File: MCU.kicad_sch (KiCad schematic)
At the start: 7 parts, among them U2 Teensy4.0, U9 W25Q128JVSIQ TR

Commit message: Finalized schematic
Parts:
- added R18, R19: 5k, Resistor_SMD:R_0402_1005Metric, symbol Device:R
- added TP1 (x13): TestPoint, TestPoint:TestPoint_Pad_1.5x1.5mm, symbol Connector:TestPoint
- C24, C25: footprint (none) -> Capacitor_SMD:C_0402_1005Metric
- R14, R24, R25: footprint (none) -> Resistor_SMD:R_0402_1005Metric
- U2: footprint (none) -> teensy:Teensy41
- U9: footprint SOIC_208MIL_WIN -> TeenieWeenieLibrary:SOIC_208MIL_WIN
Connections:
- net GNDD is gone; now on net GND: U9.4 (GND)
- net +3V3: now also R18.1, R19.1
- net ADCDAT: now also TP1.1
- net BCLK: now also TP1.1
- net CODC_IRQ: now also TP1.1
- net DACDAT: now also TP1.1
- net GND: now also U2.1 (GND)
- net MCLK: now also TP1.1
- net SCL: now also TP1.1
- net SDA: now also TP1.1
- net ~{ADC_IRQ0}: now also TP1.1
- net ~{ADC_IRQ1}: now also TP1.1
- net at U2.12 (10_CS_MQSR), U9.6 (CLK): now also TP1.1
- net at U2.13 (11_MOSI_CTX1), U9.5 (DI(IO0)): now also TP1.1
- net at U2.14 (12_MISO_MQSL), U9.2 (DO(IO1)): now also TP1.1
- net at R14.2, U2.20 (13_SCK_CRX1_LED), U9.1 (/CS): now also TP1.1
- net at U2.4 (2_OUT2): now also U9.7 (/HOLD_/RESET), R19.2
- net at U2.5 (3_LRCLK2): now also U9.3 (/WP(IO2)), R18.2
- no-connect marks 37 -> 35
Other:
- moved on the sheet: R24, R25

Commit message: final final schematic:
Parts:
- added D1: LED, LED_THT:LED_D5.0mm, symbol Device:LED
- added Q1: DMP2160UW-7, Package_TO_SOT_SMD:SOT-323_SC-70_Handsoldering, symbol Simulation_SPICE:PMOS
- added R38: 1k, Resistor_SMD:R_0402_1005Metric, symbol Device:R
- added R39: 5k, Resistor_SMD:R_0402_1005Metric, symbol Device:R
- added R40: 10k, Resistor_SMD:R_0402_1005Metric, symbol Device:R
- added SW1: SW_Push, Connector_PinHeader_1.00mm:PinHeader_1x02_P1.00mm_Vertical, symbol Switch:SW_Push
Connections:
- net +3V3: now also Q1.3 (S), R39.1, R40.1
- net GND: now also R38.2, SW1.1
- net ~{SWCTRL}: now reaches U2.6 (4_BCLK2)
- net ~{SWCTRL}: now also R39.2
- net ~{BTN}: now reaches U2.7 (5_IN2)
- net ~{BTN}: now also Q1.2 (G), R40.2, SW1.2
- new net: D1.2 (A), Q1.1 (D)
- new net: D1.1 (K), R38.1
- no-connect marks 35 -> 33

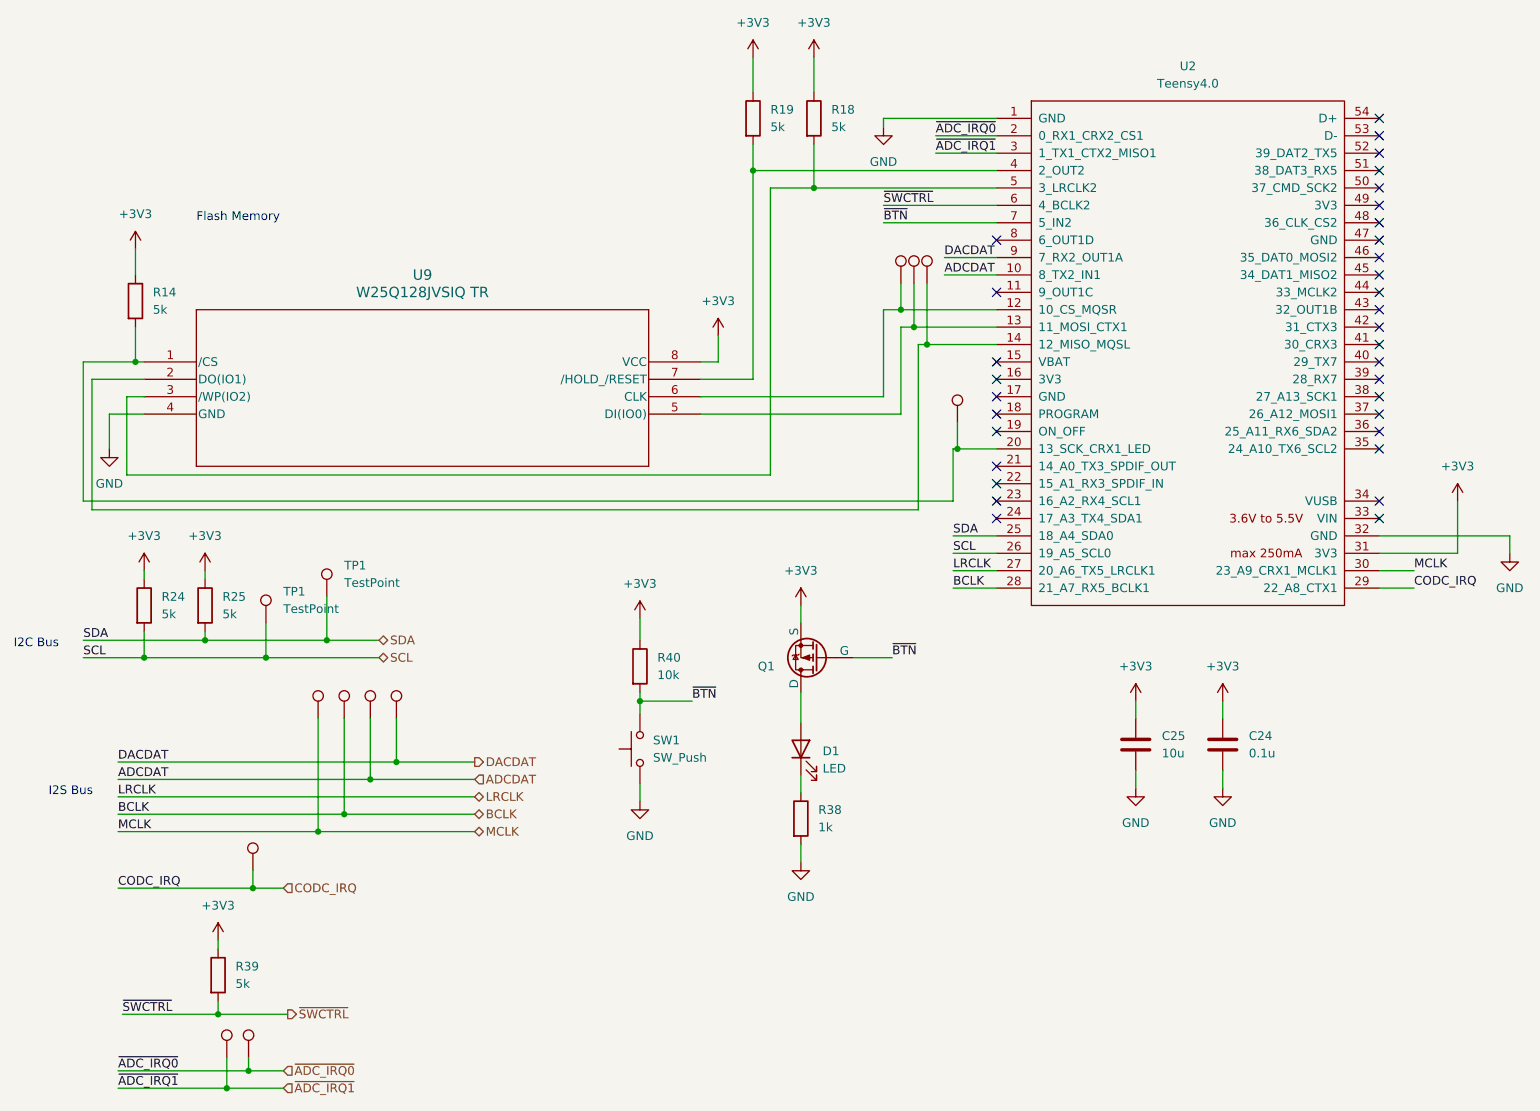
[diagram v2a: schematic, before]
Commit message: rev1 of pcb component placement
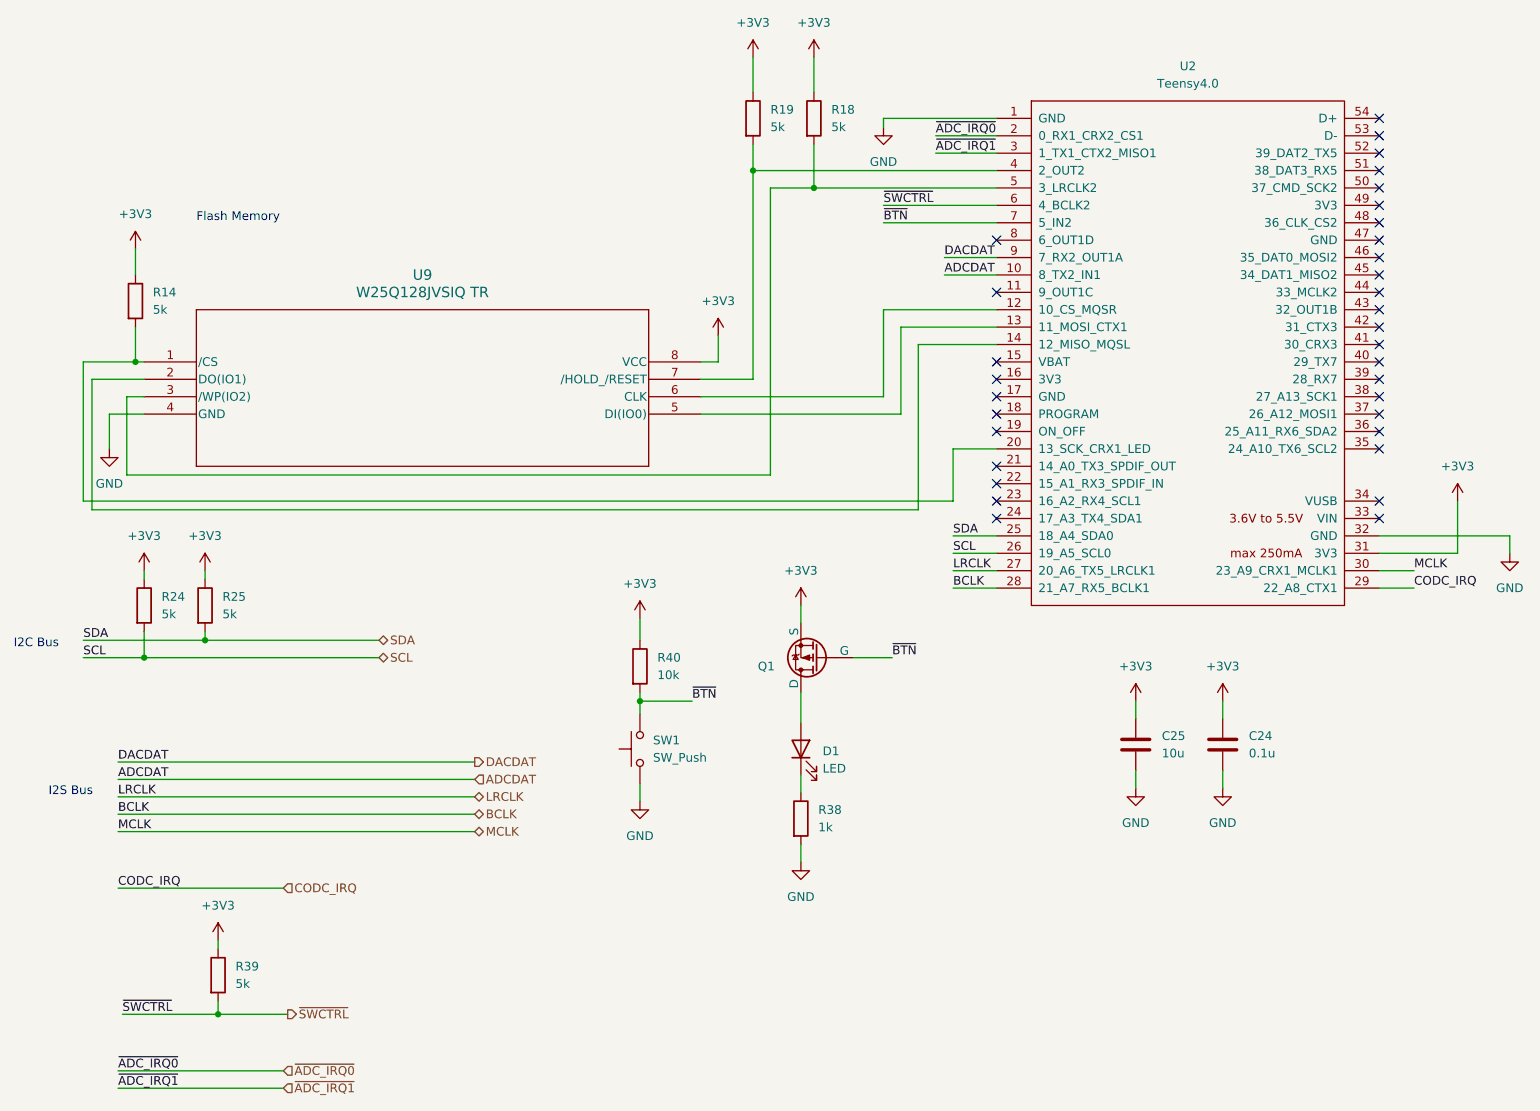
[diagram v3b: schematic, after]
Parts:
- removed TP1 (x13): TestPoint, TestPoint:TestPoint_Pad_1.5x1.5mm, symbol Connector:TestPoint
- U2: footprint teensy:Teensy41 -> teensy:Teensy40_1

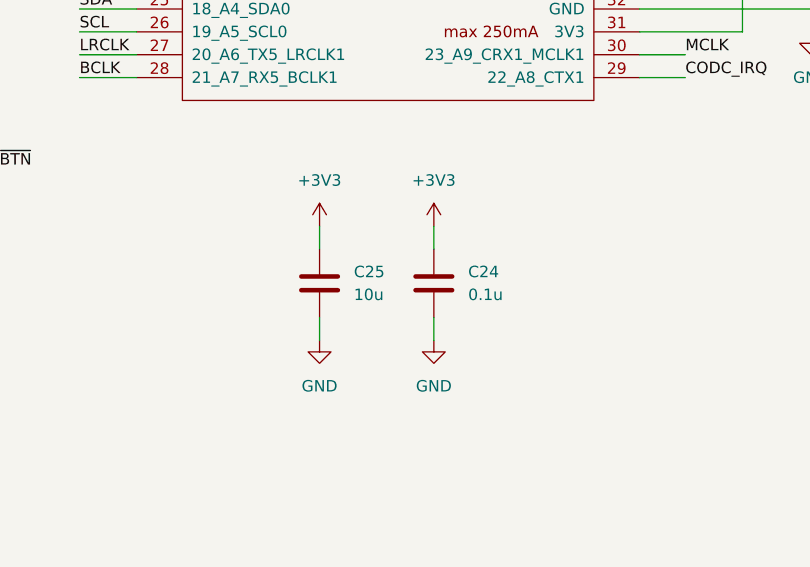
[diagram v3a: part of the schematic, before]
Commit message: routed power
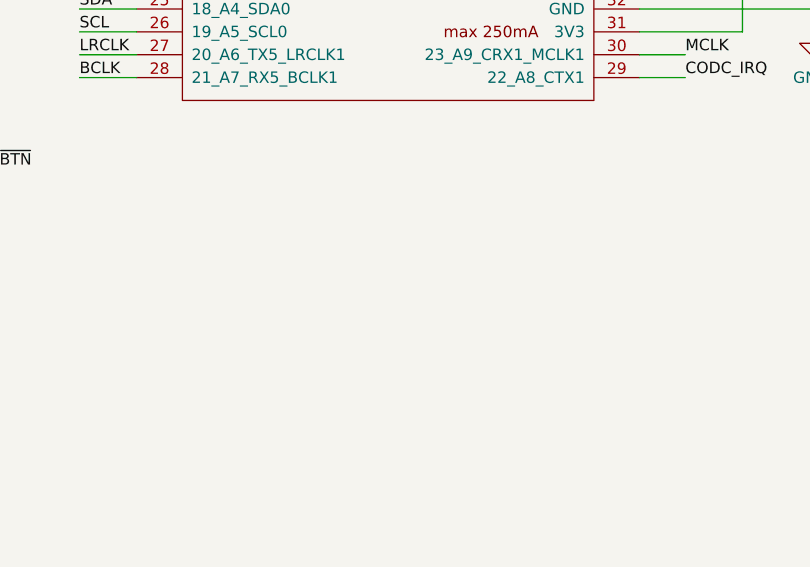
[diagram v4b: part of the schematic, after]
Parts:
- removed C24: 0.1u, Capacitor_SMD:C_0402_1005Metric, symbol Device:C
- removed C25: 10u, Capacitor_SMD:C_0402_1005Metric, symbol Device:C
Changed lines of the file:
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@@
-    (stroke (width 0) (type default))
-  )
-  (wire (pts (xy 200.66 137.16) (xy 200.66 139.7))
     (stroke (width 0) (type default))
   )
@@
     (stroke (width 0) (type default))
   )
-  (wire (pts (xy 187.96 137.16) (xy 187.96 139.7))
-    (stroke (width 0) (type default))
-  )
   (wire (pts (xy 124.46 90.17) (xy 132.08 90.17))
     (stroke (width 0) (type default))
@@
     (stroke (width 0) (type default))
   )
-  (wire (pts (xy 187.96 147.32) (xy 187.96 149.86))
-    (stroke (width 0) (type default))
-  )
   (wire (pts (xy 38.1 95.25) (xy 43.18 95.25))
     (stroke (width 0) (type default))
@@
   )
   (wire (pts (xy 115.57 149.225) (xy 115.57 151.765))
-    (stroke (width 0) (type default))
-  )
-  (wire (pts (xy 200.66 147.32) (xy 200.66 149.86))
     (stroke (width 0) (type default))
   )
@@
     )
   )
-  (symbol (lib_id "power:GND") (at 200.66 149.86 0) (unit 1)
-    (in_bom yes) (on_board yes) (dnp no) (fields_autoplaced)
-    (property "Reference" "#PWR068" (at 200.66 156.21 0)
-      (effects (font (size 1.27 1.27)) hide)
-    )
-    (property "Value" "GND" (at 200.66 154.94 0)
-      (effects (font (size 1.27 1.27)))
-    )
-    (property "Footprint" "" (at 200.66 149.86 0)
-      (effects (font (size 1.27 1.27)) hide)
-    )
-    (property "Datasheet" "" (at 200.66 149.86 0)
-      (effects (font (size 1.27 1.27)) hide)
-    )
-    (pin "1")
-    (instances
-      (project "TeenieWeenie"
-        (path "/58e2e2d3-cf30-4313-be51-7fb67401d242/db217c67-4148-46d6-b5bb-bc62bff1a084"
-          (reference "#PWR068") (unit 1)
-        )
-      )
-    )
-  )
   (symbol (lib_id "Simulation_SPICE:PMOS") (at 141.605 130.81 180) (unit 1)
     (in_bom yes) (on_board yes) (dnp no)
@@
     )
   )
-  (symbol (lib_id "power:+3V3") (at 187.96 137.16 0) (unit 1)
-    (in_bom yes) (on_board yes) (dnp no) (fields_autoplaced)
-    (property "Reference" "#PWR035" (at 187.96 140.97 0)
-      (effects (font (size 1.27 1.27)) hide)
-    )
-    (property "Value" "+3V3" (at 187.96 132.08 0)
-      (effects (font (size 1.27 1.27)))
-    )
-    (property "Footprint" "" (at 187.96 137.16 0)
-      (effects (font (size 1.27 1.27)) hide)
-    )
-    (property "Datasheet" "" (at 187.96 137.16 0)
-      (effects (font (size 1.27 1.27)) hide)
-    )
-    (pin "1")
-    (instances
-      (project "TeenieWeenie"
-        (path "/58e2e2d3-cf30-4313-be51-7fb67401d242/d79052ad-b30d-48cb-904a-b15d582d373d"
-          (reference "#PWR035") (unit 1)
-        )
-        (path "/58e2e2d3-cf30-4313-be51-7fb67401d242/db217c67-4148-46d6-b5bb-bc62bff1a084"
-          (reference "#PWR065") (unit 1)
-        )
-      )
-    )
-  )
   (symbol (lib_id "power:+3V3") (at 52.07 118.11 0) (unit 1)
     (in_bom yes) (on_board yes) (dnp no) (fields_autoplaced)
@@
     )
   )
-  (symbol (lib_id "power:+3V3") (at 200.66 137.16 0) (unit 1)
-    (in_bom yes) (on_board yes) (dnp no) (fields_autoplaced)
-    (property "Reference" "#PWR033" (at 200.66 140.97 0)
-      (effects (font (size 1.27 1.27)) hide)
-    )
-    (property "Value" "+3V3" (at 200.66 132.08 0)
-      (effects (font (size 1.27 1.27)))
-    )
-    (property "Footprint" "" (at 200.66 137.16 0)
-      (effects (font (size 1.27 1.27)) hide)
-    )
-    (property "Datasheet" "" (at 200.66 137.16 0)
-      (effects (font (size 1.27 1.27)) hide)
-    )
-    (pin "1")
-    (instances
-      (project "TeenieWeenie"
-        (path "/58e2e2d3-cf30-4313-be51-7fb67401d242/d79052ad-b30d-48cb-904a-b15d582d373d"
-          (reference "#PWR033") (unit 1)
-        )
-        (path "/58e2e2d3-cf30-4313-be51-7fb67401d242/db217c67-4148-46d6-b5bb-bc62bff1a084"
-          (reference "#PWR067") (unit 1)
-        )
-      )
-    )
-  )
   (symbol (lib_id "Device:R") (at 41.91 78.74 0) (unit 1)
     (in_bom yes) (on_board yes) (dnp no) (fields_autoplaced)
@@
     )
   )
-  (symbol (lib_id "Device:C") (at 200.66 143.51 0) (unit 1)
-    (in_bom yes) (on_board yes) (dnp no) (fields_autoplaced)
-    (property "Reference" "C24" (at 204.47 142.24 0)
-      (effects (font (size 1.27 1.27)) (justify left))
-    )
-    (property "Value" "0.1u" (at 204.47 144.78 0)
-      (effects (font (size 1.27 1.27)) (justify left))
-    )
-    (property "Footprint" "Capacitor_SMD:C_0402_1005Metric" (at 201.6252 147.32 0)
-      (effects (font (size 1.27 1.27)) hide)
-    )
-    (property "Datasheet" "~" (at 200.66 143.51 0)
-      (effects (font (size 1.27 1.27)) hide)
-    )
-    (pin "1")
-    (pin "2")
-    (instances
-      (project "TeenieWeenie"
-        (path "/58e2e2d3-cf30-4313-be51-7fb67401d242/d79052ad-b30d-48cb-904a-b15d582d373d"
-          (reference "C24") (unit 1)
-        )
-        (path "/58e2e2d3-cf30-4313-be51-7fb67401d242/db217c67-4148-46d6-b5bb-bc62bff1a084"
-          (reference "C46") (unit 1)
-        )
-      )
-    )
-  )
   (symbol (lib_id "Device:R") (at 139.065 154.305 0) (unit 1)
     (in_bom yes) (on_board yes) (dnp no) (fields_autoplaced)
@@
     )
   )
-  (symbol (lib_id "Device:C") (at 187.96 143.51 0) (unit 1)
-    (in_bom yes) (on_board yes) (dnp no) (fields_autoplaced)
-    (property "Reference" "C25" (at 191.77 142.24 0)
-      (effects (font (size 1.27 1.27)) (justify left))
-    )
-    (property "Value" "10u" (at 191.77 144.78 0)
-      (effects (font (size 1.27 1.27)) (justify left))
-    )
-    (property "Footprint" "Capacitor_SMD:C_0402_1005Metric" (at 188.9252 147.32 0)
-      (effects (font (size 1.27 1.27)) hide)
-    )
-    (property "Datasheet" "~" (at 187.96 143.51 0)
-      (effects (font (size 1.27 1.27)) hide)
-    )
-    (pin "1")
-    (pin "2")
-    (instances
-      (project "TeenieWeenie"
-        (path "/58e2e2d3-cf30-4313-be51-7fb67401d242/d79052ad-b30d-48cb-904a-b15d582d373d"
-          (reference "C25") (unit 1)
-        )
-        (path "/58e2e2d3-cf30-4313-be51-7fb67401d242/db217c67-4148-46d6-b5bb-bc62bff1a084"
-          (reference "C22") (unit 1)
-        )
-      )
-    )
-  )
   (symbol (lib_id "Device:R") (at 43.18 123.19 0) (unit 1)
     (in_bom yes) (on_board yes) (dnp no) (fields_autoplaced)
@@
         )
       )
-    )
-  )
-  (symbol (lib_id "power:GND") (at 187.96 149.86 0) (unit 1)
-    (in_bom yes) (on_board yes) (dnp no) (fields_autoplaced)
-    (property "Reference" "#PWR066" (at 187.96 156.21 0)
-      (effects (font (size 1.27 1.27)) hide)
-    )
-    (property "Value" "GND" (at 187.96 154.94 0)
-      (effects (font (size 1.27 1.27)))
-    )
-    (property "Footprint" "" (at 187.96 149.86 0)
-      (effects (font (size 1.27 1.27)) hide)
-    )
-    (property "Datasheet" "" (at 187.96 149.86 0)
-      (effects (font (size 1.27 1.27)) hide)
-    )
-    (pin "1")
-    (instances
-      (project "TeenieWeenie"
-        (path "/58e2e2d3-cf30-4313-be51-7fb67401d242/db217c67-4148-46d6-b5bb-bc62bff1a084"
-          (reference "#PWR066") (unit 1)
-        )
-      )
